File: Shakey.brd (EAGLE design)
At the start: 146.4 x 62.1 mm, 84 parts, among them CN1 CONN_USB-4UCON-11071, U1 ATMEGA32U4-AU, U2 ICM-20689, U3 AP2210K-3.3TRG1, U4 LM75AD, Y1 16Mhz

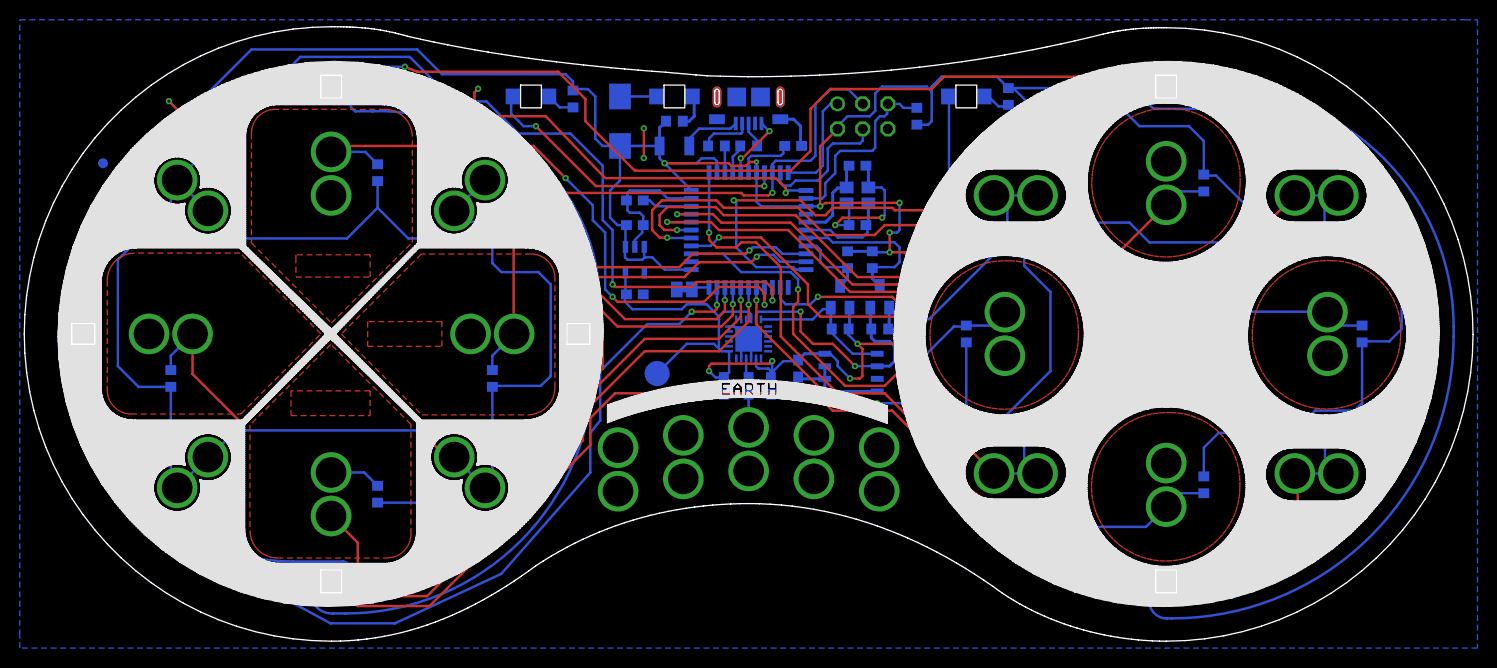
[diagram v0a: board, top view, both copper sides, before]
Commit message: changed croc hole to 3.0mm
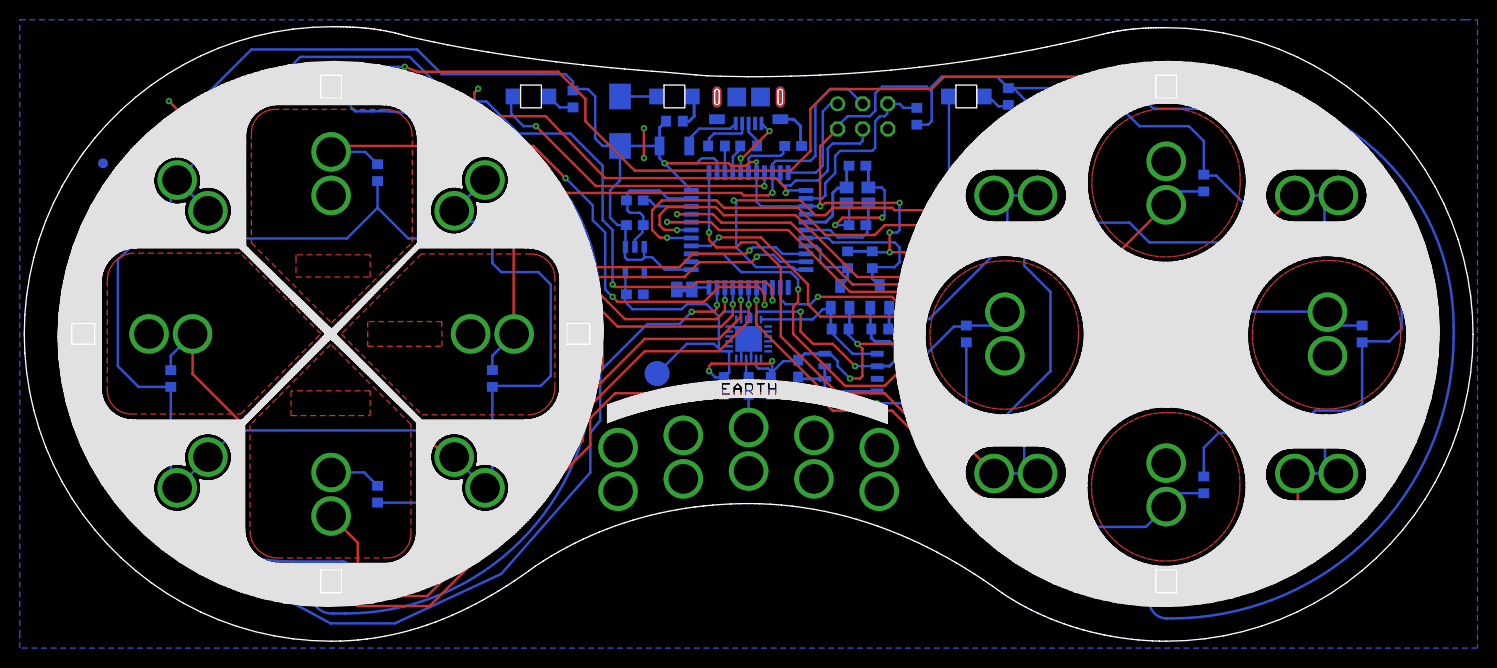
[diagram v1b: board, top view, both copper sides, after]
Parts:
- A, CLICK, DOWN, EARTH1, EARTH2, EARTH3, EARTH4, EARTH5, F, G, LEFT, MOUSE-DOWN, MOUSE-LEFT, MOUSE-LEFT-CLICK, MOUSE-RIGHT, MOUSE-RIGHT-CLICK, MOUSE-UP, RIGHT, SPACE, UP, W: value (none) -> MA01-1-ALLIGATOR-3.0MM; device SixthLogic:MA01-1-ALLIGATOR-3.1MM -> SixthLogic:MA01-1-ALLIGATOR-3.0MM

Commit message: correct Micro USB value for P&P
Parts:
- CN1: value CONN_USB-4UCON-11071 -> MicroUSB; device SixthLogic:CONN_USB_MICRO_B_4UCON-11071 -> SixthLogic:4UCON-11071
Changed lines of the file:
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@@
 <attribute name="URL" value="https://www.digikey.com/product-detail/en/samsung-electro-mechanics/CL10B104KB8NNNC/1276-1000-2-ND/3886658" x="-11.5" y="13.5" size="1.778" layer="28" rot="MR180" display="off"/>
 </element>
-<element name="CN1" library="SixthLogic" package="CONN_USB_MICRO_B_4UCON-11071" value="CONN_USB-4UCON-11071" x="0" y="25.4" smashed="yes" rot="MR180">
+<element name="CN1" library="SixthLogic" package="4UCON-11071" value="MicroUSB" x="0" y="25.4" smashed="yes" rot="MR180">
 <attribute name="DESCRIPTION" value="B TYPE FEMALE 05P SMT 90° WITHOUT POST 2 SHELL TABS" x="34.29" y="44.45" size="1.778" layer="28" rot="MR180" display="off"/>
 <attribute name="MPN" value="11071" x="34.29" y="44.45" size="1.778" layer="28" rot="MR180" display="off"/>

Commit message: added part value for P&P
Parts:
- A, CLICK, DOWN, EARTH1, EARTH2, EARTH3, EARTH4, EARTH5, F, G, LEFT, MOUSE-DOWN, MOUSE-LEFT, MOUSE-LEFT-CLICK, MOUSE-RIGHT, MOUSE-RIGHT-CLICK, MOUSE-UP, RIGHT, SPACE, UP, W: value MA01-1-ALLIGATOR-3.0MM -> (none)
- turned PC1 to 0 degrees
- turned U4 to 0 degrees
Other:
- board text added: "JLCJLCJLCJLC"

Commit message: changed name to ShakeUp
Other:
- board text added: "SKU : LB-SHAKEUP-1"
- board text added: "ShakeUp"
- board text added: "Version 1.1"
- board text removed: "SKU : LB-SHAKEY-1"
- board text removed: "Shakey"
- board text removed: "Version 1.0"
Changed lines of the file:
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@@
 <grid distance="9.84251969" unitdist="mil" unit="mil" style="lines" multiple="1" display="yes" altdistance="0.01" altunitdist="mm" altunit="mm"/>
 <layers>
-<layer number="1" name="Top" color="4" fill="1" visible="yes" active="yes"/>
+<layer number="1" name="Top" color="4" fill="1" visible="no" active="yes"/>
 <layer number="2" name="Route2" color="1" fill="3" visible="no" active="no"/>
 <layer number="3" name="Route3" color="4" fill="3" visible="no" active="no"/>
@@
 <layer number="19" name="Unrouted" color="6" fill="1" visible="yes" active="yes"/>
 <layer number="20" name="Dimension" color="15" fill="1" visible="yes" active="yes"/>
-<layer number="21" name="tPlace" color="7" fill="1" visible="yes" active="yes"/>
+<layer number="21" name="tPlace" color="7" fill="1" visible="no" active="yes"/>
 <layer number="22" name="bPlace" color="7" fill="1" visible="yes" active="yes"/>
 <layer number="23" name="tOrigins" color="15" fill="1" visible="yes" active="yes"/>
@@
 <layer number="27" name="tValues" color="7" fill="1" visible="yes" active="yes"/>
 <layer number="28" name="bValues" color="7" fill="1" visible="no" active="yes"/>
-<layer number="29" name="tStop" color="7" fill="3" visible="yes" active="yes"/>
+<layer number="29" name="tStop" color="7" fill="3" visible="no" active="yes"/>
 <layer number="30" name="bStop" color="7" fill="6" visible="yes" active="yes"/>
-<layer number="31" name="tCream" color="10" fill="4" visible="yes" active="yes"/>
+<layer number="31" name="tCream" color="10" fill="4" visible="no" active="yes"/>
 <layer number="32" name="bCream" color="7" fill="5" visible="yes" active="yes"/>
-<layer number="33" name="tFinish" color="6" fill="3" visible="yes" active="yes"/>
+<layer number="33" name="tFinish" color="6" fill="3" visible="no" active="yes"/>
 <layer number="34" name="bFinish" color="6" fill="6" visible="yes" active="yes"/>
 <layer number="35" name="tGlue" color="7" fill="4" visible="yes" active="yes"/>
@@
 <layer number="37" name="tTest" color="7" fill="1" visible="yes" active="yes"/>
 <layer number="38" name="bTest" color="7" fill="1" visible="yes" active="yes"/>
-<layer number="39" name="tKeepout" color="4" fill="11" visible="yes" active="yes"/>
+<layer number="39" name="tKeepout" color="4" fill="11" visible="no" active="yes"/>
 <layer number="40" name="bKeepout" color="1" fill="11" visible="yes" active="yes"/>
-<layer number="41" name="tRestrict" color="4" fill="10" visible="yes" active="yes"/>
+<layer number="41" name="tRestrict" color="4" fill="10" visible="no" active="yes"/>
 <layer number="42" name="bRestrict" color="1" fill="10" visible="yes" active="yes"/>
 <layer number="43" name="vRestrict" color="2" fill="10" visible="yes" active="yes"/>
@@
 <wire x1="19.5" y1="25" x2="19.2" y2="25.3" width="0.3" layer="201" curve="106.260205"/>
 <wire x1="19.2" y1="25.3" x2="19" y2="25.8" width="0.3" layer="201" curve="-138.780451"/>
-<text x="-42" y="7.1" size="2.54" layer="22" ratio="12" rot="MR0" align="center">Shakey</text>
+<text x="-42" y="7.1" size="2.54" layer="22" ratio="12" rot="MR0" align="center">ShakeUp</text>
 <wire x1="-35.25" y1="4.5" x2="-48.5" y2="4.5" width="0.3" layer="22"/>
 <text x="-42" y="3" size="1.016" layer="22" font="vector" ratio="12" rot="MR0" align="center">Manufactured in Australia</text>
 <text x="-42" y="-1.5" size="1.27" layer="22" font="vector" ratio="16" rot="MR0" align="center">Little Bird Co</text>
-<text x="-42" y="-4.5" size="1.016" layer="22" font="vector" ratio="12" rot="MR0" align="center">Version 1.0</text>
-<text x="-42" y="-6.75" size="1.016" layer="22" font="vector" ratio="12" rot="MR0" align="center">SKU : LB-SHAKEY-1</text>
+<text x="-42" y="-4.5" size="1.016" layer="22" font="vector" ratio="12" rot="MR0" align="center">Version 1.1</text>
+<text x="-42" y="-6.75" size="1.016" layer="22" font="vector" ratio="12" rot="MR0" align="center">SKU : LB-SHAKEUP-1</text>
 <text x="42.75" y="6.75" size="2.54" layer="22" ratio="12" rot="MR0" align="center">WebUSB</text>
 <wire x1="53" y1="4.5" x2="32.25" y2="4.5" width="0.3" layer="22"/>
